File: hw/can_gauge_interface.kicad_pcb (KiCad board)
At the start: 2 copper layers, 58 parts, among them J1 USB_B, J10 Conn_01x01_Socket, J2 Conn_02x04_Top_Bottom, J3 Analog, J4 ICSP, J5 SPI debug, J6 Conn_01x01_Socket, J7 Conn_01x01_Socket, J8 Conn_01x01_Socket, J9 Conn_01x01_Socket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

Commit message: layout
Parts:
- R10, R11, R4, R6, R7, R9: footprint Resistor_SMD:R_0805_2012Metric_Pad1.20x1.40mm_HandSolder -> Resistor_THT:R_Axial_DIN0411_L9.9mm_D3.6mm_P12.70mm_Horizontal
- moved H1 344.1 mm to (33.0, 58.0)
- moved JP5 212.7 mm to (55.9, 134.6), turned to 180 degrees
- moved R8 200.3 mm to (49.8, 132.1), turned to 180 degrees
- moved R7 146.5 mm to (104.1, 121.9), turned to -90 degrees
- moved C14 145.3 mm to (78.7, 137.2), turned to 90 degrees
- moved C13 129.1 mm to (94.0, 127.0)
- moved J5 115.4 mm to (383.5, 59.3)
- moved JP3 109.4 mm to (368.3, 124.5)
- moved JP4 109.4 mm to (370.8, 111.8)
- moved J10 100.7 mm to (364.0, 77.7)
- moved J6 100.7 mm to (364.0, 59.3)
- moved J7 100.7 mm to (364.0, 63.9)
- moved J8 100.7 mm to (364.0, 68.5)
- moved J9 100.7 mm to (364.0, 73.1)
- moved R9 95.2 mm to (154.9, 142.2), turned to 180 degrees
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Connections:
- net Net-(U2-RXCAN) renamed /CAN_RX
- net Net-(U2-TXCAN) renamed /CAN_TX
- J2 pad 1: +12V -> /Tach
- J2 pad 4: /Tach -> +12V
- J2 pad 5: GND -> /Speed
- J2 pad 8: /Speed -> GND
- JP2 pad 1: Net-(JP2-A) -> /INT
- JP2 pad 2: /INT -> /INT/ICSP_CLK
- U1 pad 10: /DAC1_~{CS} -> unconnected-(U1-RB7/TX/CK-Pad10)
- U1 pad 12: /CAN_~{CS} -> unconnected-(U1-RB5/AN11/RX/DX-Pad12)
- U1 pad 14: /DAC2_~{CS} -> unconnected-(U1-C2IN2-/C1IN2-/DACOUT1/AN6/RC2-Pad14)
- U1 pad 15: Net-(JP2-A) -> /INT/ICSP_CLK
- U1 pad 2: /ROM_~{CS} -> unconnected-(U1-RA5/SOSCI/T1CKI/OSC1/CLKIN-Pad2)

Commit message: dac pullup layout
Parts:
- moved R11 286.0 mm to (73.7, 226.1), turned to 90 degrees
- moved R10 248.9 mm to (101.6, 226.1), turned to 90 degrees
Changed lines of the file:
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@@
 		(tags "THT DIP DIL PDIP 2.54mm 7.62mm 300mil")
 		(property "Reference" "U8"
-			(at -2.54 0 180)
+			(at 10.16 3.81 180)
 			(layer "F.SilkS")
 			(effects
@@
 	(footprint "Resistor_THT:R_Axial_DIN0411_L9.9mm_D3.6mm_P12.70mm_Horizontal"
 		(layer "F.Cu")
-		(at 327.66 121.92)
+		(at 101.6 226.06 90)
 		(descr "Resistor, Axial_DIN0411 series, Axial, Horizontal, pin pitch=12.7mm, 1W, length*diameter=9.9*3.6mm^2")
 		(tags "Resistor Axial_DIN0411 series Axial Horizontal pin pitch 12.7mm 1W length 9.9mm diameter 3.6mm")
 		(property "Reference" "R10"
-			(at 6.35 -2.92 0)
+			(at 5.08 5.08 180)
 			(layer "F.SilkS")
 			(effects
@@
 		)
 		(property "Value" "10k"
-			(at 6.35 2.92 0)
+			(at 6.35 2.92 90)
 			(layer "F.Fab")
+			(hide yes)
 			(effects
 				(font
@@
 		)
 		(property "Datasheet" ""
-			(at 0 0 0)
+			(at 0 0 90)
 			(unlocked yes)
 			(layer "F.Fab")
@@
 		)
 		(property "Description" "Resistor, US symbol"
-			(at 0 0 0)
+			(at 0 0 90)
 			(unlocked yes)
 			(layer "F.Fab")
@@
 		(attr through_hole)
 		(fp_line
-			(start 1.28 -1.92)
-			(end 11.42 -1.92)
+			(start 11.42 -1.92)
+			(end 11.42 -1.44)
 			(stroke
 				(width 0.12)
@@
 		)
 		(fp_line
-			(start 1.28 -1.44)
-			(end 1.28 -1.92)
+			(start 1.28 -1.92)
+			(end 11.42 -1.92)
 			(stroke
 				(width 0.12)
@@
 		)
 		(fp_line
-			(start 1.28 1.44)
-			(end 1.28 1.92)
+			(start 1.28 -1.44)
+			(end 1.28 -1.92)
 			(stroke
 				(width 0.12)
@@
 		)
 		(fp_line
-			(start 1.28 1.92)
-			(end 11.42 1.92)
+			(start 1.28 1.44)
+			(end 1.28 1.92)
 			(stroke
 				(width 0.12)
@@
 		)
 		(fp_line
-			(start 11.42 -1.92)
-			(end 11.42 -1.44)
+			(start 11.42 1.92)
+			(end 11.42 1.44)
 			(stroke
 				(width 0.12)
@@
 		)
 		(fp_line
-			(start 11.42 1.92)
-			(end 11.42 1.44)
+			(start 1.28 1.92)
+			(end 11.42 1.92)
 			(stroke
 				(width 0.12)
@@
 		)
 		(fp_line
-			(start -1.45 -2.05)
-			(end -1.45 2.05)
+			(start 14.15 -2.05)
+			(end -1.45 -2.05)
 			(stroke
 				(width 0.05)
@@
 		)
 		(fp_line
-			(start -1.45 2.05)
-			(end 14.15 2.05)
+			(start -1.45 -2.05)
+			(end -1.45 2.05)
 			(stroke
 				(width 0.05)
@@
 		)
 		(fp_line
-			(start 14.15 -2.05)
-			(end -1.45 -2.05)
+			(start 14.15 2.05)
+			(end 14.15 -2.05)
 			(stroke
 				(width 0.05)
@@
 		)
 		(fp_line
-			(start 14.15 2.05)
-			(end 14.15 -2.05)
+			(start -1.45 2.05)
+			(end 14.15 2.05)
 			(stroke
 				(width 0.05)
@@
 		)
 		(fp_line
-			(start 0 0)
-			(end 1.4 0)
+			(start 11.3 -1.8)
+			(end 1.4 -1.8)
 			(stroke
 				(width 0.1)
@@
 		)
 		(fp_line
-			(start 1.4 1.8)
-			(end 11.3 1.8)
+			(start 12.7 0)
+			(end 11.3 0)
 			(stroke
 				(width 0.1)
@@
 		)
 		(fp_line
-			(start 11.3 -1.8)
-			(end 1.4 -1.8)
+			(start 0 0)
+			(end 1.4 0)
 			(stroke
 				(width 0.1)
@@
 		)
 		(fp_line
-			(start 12.7 0)
-			(end 11.3 0)
+			(start 1.4 1.8)
+			(end 11.3 1.8)
 			(stroke
 				(width 0.1)
@@
 		)
 		(fp_text user "${REFERENCE}"
-			(at 6.35 0 0)
+			(at 6.35 0 90)
 			(layer "F.Fab")
 			(effects
@@
 		)
 		(pad "1" thru_hole circle
-			(at 0 0)
+			(at 0 0 90)
 			(size 2.4 2.4)
 			(drill 1.2)
@@
 		)
 		(pad "2" thru_hole oval
-			(at 12.7 0)
+			(at 12.7 0 90)
 			(size 2.4 2.4)
 			(drill 1.2)
@@
 	(footprint "Resistor_THT:R_Axial_DIN0411_L9.9mm_D3.6mm_P12.70mm_Horizontal"
 		(layer "F.Cu")
-		(at 342.9 129.54)
+		(at 73.66 226.06 90)
 		(descr "Resistor, Axial_DIN0411 series, Axial, Horizontal, pin pitch=12.7mm, 1W, length*diameter=9.9*3.6mm^2")
 		(tags "Resistor Axial_DIN0411 series Axial Horizontal pin pitch 12.7mm 1W length 9.9mm diameter 3.6mm")
 		(property "Reference" "R11"
-			(at 6.35 -2.92 0)
+			(at 5.08 5.08 180)
 			(layer "F.SilkS")
 			(effects
@@
 		)
 		(property "Value" "10k"
-			(at 6.35 2.92 0)
+			(at 6.35 2.92 90)
 			(layer "F.Fab")
+			(hide yes)
 			(effects
 				(font
@@
 		)
 		(property "Datasheet" ""
-			(at 0 0 0)
+			(at 0 0 90)
 			(unlocked yes)
 			(layer "F.Fab")
@@
 		)
 		(property "Description" "Resistor, US symbol"
-			(at 0 0 0)
+			(at 0 0 90)
 			(unlocked yes)
 			(layer "F.Fab")
@@
 		(attr through_hole)
 		(fp_line
-			(start 1.28 -1.92)
-			(end 11.42 -1.92)
+			(start 11.42 -1.92)
+			(end 11.42 -1.44)
 			(stroke
 				(width 0.12)
@@
 		)
 		(fp_line
-			(start 1.28 -1.44)
-			(end 1.28 -1.92)
+			(start 1.28 -1.92)
+			(end 11.42 -1.92)
 			(stroke
 				(width 0.12)
@@
 		)
 		(fp_line
-			(start 1.28 1.44)
-			(end 1.28 1.92)
+			(start 1.28 -1.44)
+			(end 1.28 -1.92)
 			(stroke
 				(width 0.12)
@@
 		)
 		(fp_line
-			(start 1.28 1.92)
-			(end 11.42 1.92)
+			(start 1.28 1.44)
+			(end 1.28 1.92)
 			(stroke
 				(width 0.12)
@@
 		)
 		(fp_line
-			(start 11.42 -1.92)
-			(end 11.42 -1.44)
+			(start 11.42 1.92)
+			(end 11.42 1.44)
 			(stroke
 				(width 0.12)
@@
 		)
 		(fp_line
-			(start 11.42 1.92)
-			(end 11.42 1.44)
+			(start 1.28 1.92)
+			(end 11.42 1.92)
 			(stroke
 				(width 0.12)
@@
 		)
 		(fp_line
-			(start -1.45 -2.05)
-			(end -1.45 2.05)
+			(start 14.15 -2.05)
+			(end -1.45 -2.05)
 			(stroke
 				(width 0.05)
@@
 		)
 		(fp_line
-			(start -1.45 2.05)
-			(end 14.15 2.05)
+			(start -1.45 -2.05)
+			(end -1.45 2.05)
 			(stroke
 				(width 0.05)
@@
 		)
 		(fp_line
-			(start 14.15 -2.05)
-			(end -1.45 -2.05)
+			(start 14.15 2.05)
+			(end 14.15 -2.05)
 			(stroke
 				(width 0.05)
@@
 		)
 		(fp_line
-			(start 14.15 2.05)
-			(end 14.15 -2.05)
+			(start -1.45 2.05)
+			(end 14.15 2.05)
 			(stroke
 				(width 0.05)
@@
 		)
 		(fp_line
-			(start 0 0)
-			(end 1.4 0)
+			(start 11.3 -1.8)
+			(end 1.4 -1.8)
 			(stroke
 				(width 0.1)
@@
 		)
 		(fp_line
-			(start 1.4 1.8)
-			(end 11.3 1.8)
+			(start 12.7 0)
+			(end 11.3 0)
 			(stroke
 				(width 0.1)
@@
 		)
 		(fp_line
-			(start 11.3 -1.8)
-			(end 1.4 -1.8)
+			(start 0 0)
+			(end 1.4 0)
 			(stroke
 				(width 0.1)
@@
 		)
 		(fp_line
-			(start 12.7 0)
-			(end 11.3 0)
+			(start 1.4 1.8)
+			(end 11.3 1.8)
 			(stroke
 				(width 0.1)
@@
 		)
 		(fp_text user "${REFERENCE}"
-			(at 6.35 0 0)
+			(at 6.35 0 90)
 			(layer "F.Fab")
 			(effects
@@
 		)
 		(pad "1" thru_hole circle
-			(at 0 0)
+			(at 0 0 90)
 			(size 2.4 2.4)
 			(drill 1.2)
@@
 		)
 		(pad "2" thru_hole oval
-			(at 12.7 0)
+			(at 12.7 0 90)
 			(size 2.4 2.4)
 			(drill 1.2)
@@
 		(tags "THT DIP DIL PDIP 2.54mm 7.62mm 300mil")
 		(property "Reference" "U9"
-			(at -2.54 0 180)
+			(at 10.16 2.54 180)
 			(layer "F.SilkS")
 			(effects

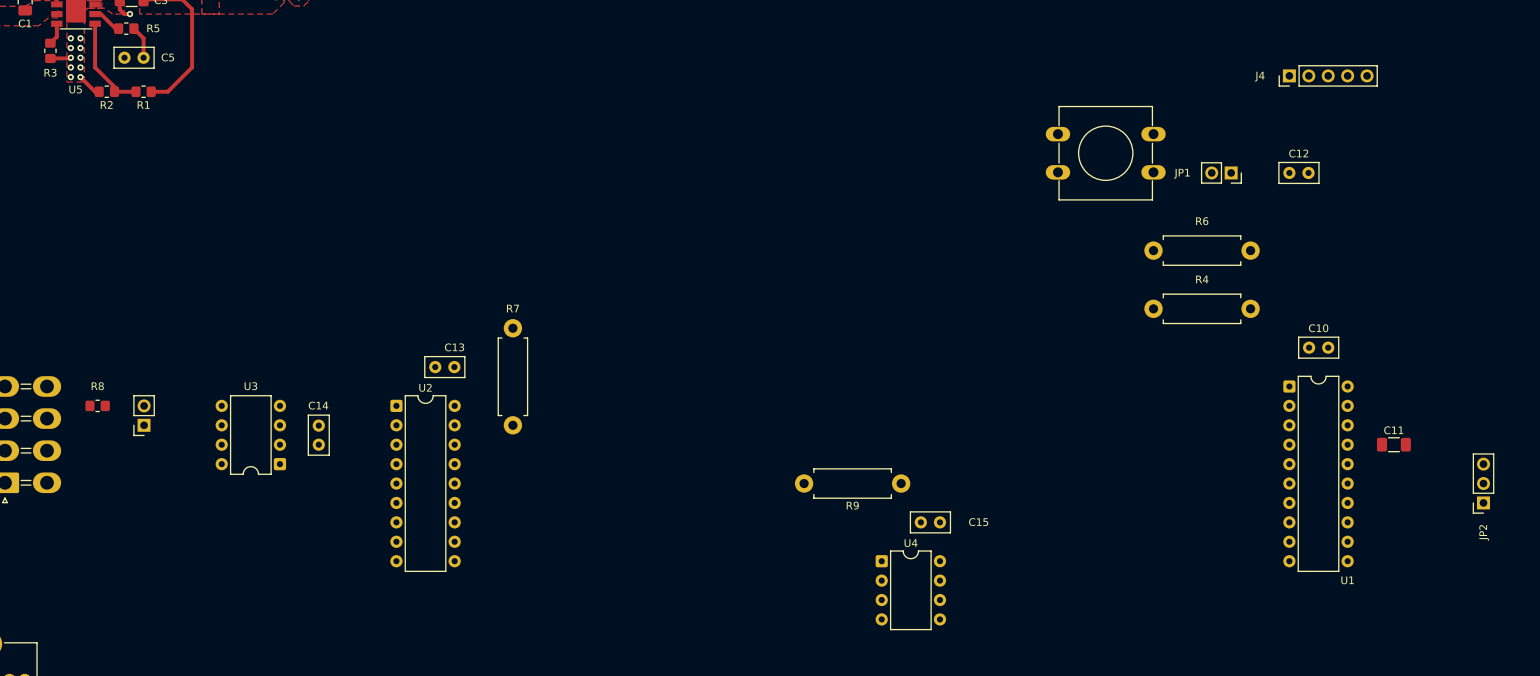
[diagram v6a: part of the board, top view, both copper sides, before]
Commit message: 4 layer stackup and CAN routing
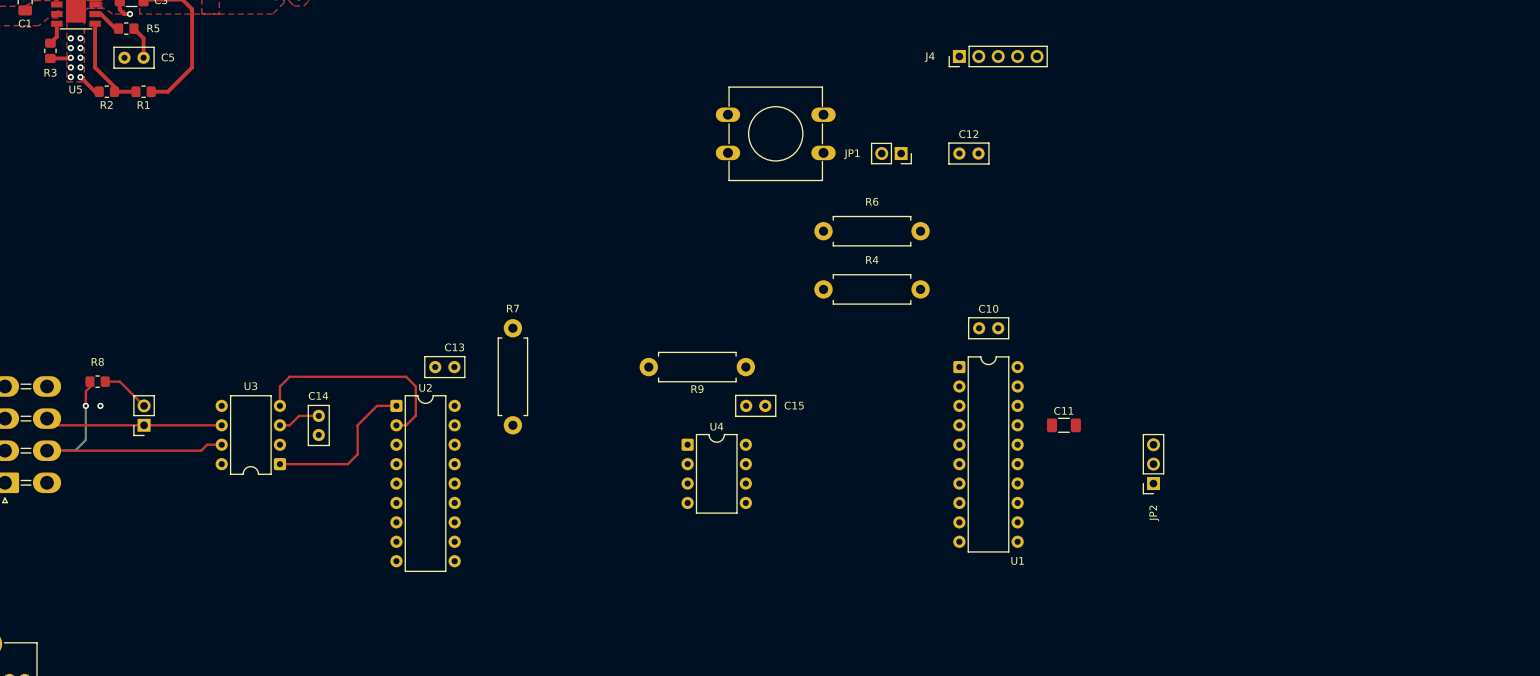
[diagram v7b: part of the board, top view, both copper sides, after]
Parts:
- moved C10 43.3 mm to (165.1, 121.9)
- moved C12 43.3 mm to (162.6, 99.1)
- moved J4 43.3 mm to (162.6, 86.4)
- moved JP1 43.3 mm to (154.9, 99.1)
- moved R4 43.3 mm to (144.8, 116.8)
- moved R6 43.3 mm to (157.5, 109.2)
- moved SW1 43.3 mm to (132.3, 94.0)
- moved U1 43.3 mm to (162.6, 127.0)
- moved C11 43.3 mm to (176.2, 134.6)
- moved JP2 43.3 mm to (188.0, 142.2)
- moved U4 29.6 mm to (127.0, 137.2)
- moved C15 27.5 mm to (137.2, 132.1)
- moved R9 25.4 mm to (134.6, 127.0)
- moved R8 3.18 mm to (49.8, 128.9)
- moved C14 1.27 mm to (78.7, 135.9)
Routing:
- net /CAN_H: track 0.00 -> 36.7 mm, vias 0 -> 1
- net /CAN_RX: track 0.00 -> 28.2 mm
- net /CAN_L: track 0.00 -> 23.2 mm
- net /CAN_TX: track 0.00 -> 20.6 mm
- net Net-(JP5-B): track 0.00 -> 6.40 mm
- net +5V: track 0.00 -> 5.59 mm
- net GND: vias 49 -> 50
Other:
- copper layers 2 -> 4

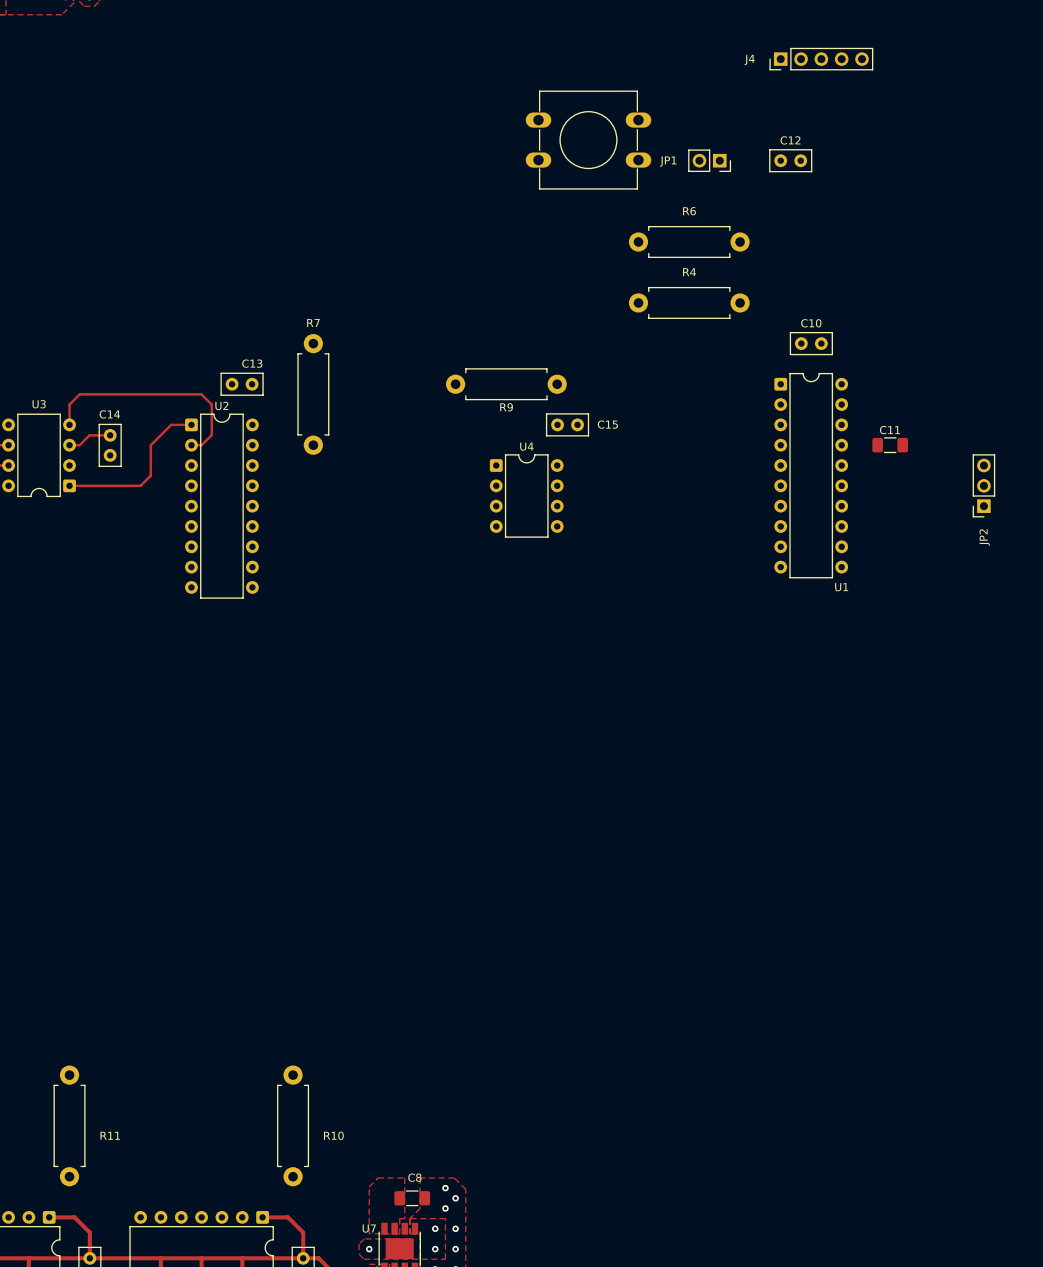
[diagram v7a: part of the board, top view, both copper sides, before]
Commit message: spi routing
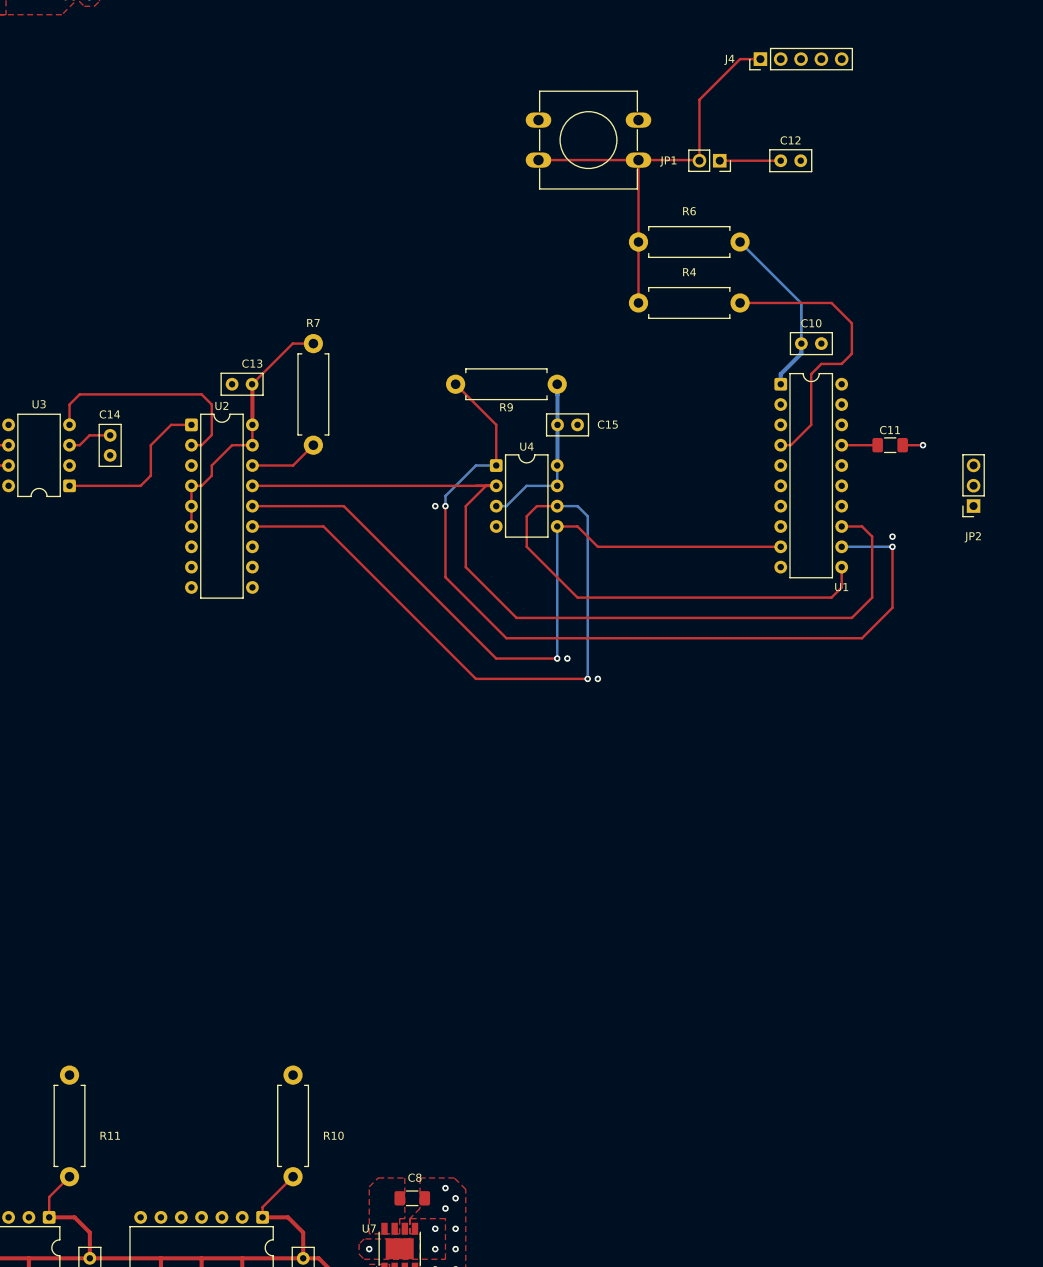
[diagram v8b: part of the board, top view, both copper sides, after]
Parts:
- moved J4 2.54 mm to (160.0, 86.4)
- moved JP2 1.30 mm to (186.7, 142.2)
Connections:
- U1 pad 12: unconnected-(U1-RB5/AN11/RX/DX-Pad12) -> /ROM_~{CS}
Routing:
- net /SCK: track 0.00 -> 127.7 mm, vias 0 -> 1
- net /MISO: track 0.00 -> 111.9 mm
- net /ROM_~{CS}: track 0.00 -> 104.9 mm, vias 0 -> 2
- net /MOSI: track 0.00 -> 91.5 mm, vias 0 -> 1
- net +5V: track 5.59 -> 82.0 mm
- net /ICSP_~{MCLR}: track 0.00 -> 55.4 mm
- net /~{MCLR}: track 0.00 -> 36.2 mm
- net +5VA: track 87.6 -> 100.4 mm
- net /CAN_~{CS}: track 0.00 -> 8.67 mm
- net Net-(JP1-A): track 0.00 -> 7.62 mm
- net Net-(U1-Vusb3v3): track 0.00 -> 4.50 mm
- net GND: track 8.85 -> 11.4 mm, vias 50 -> 55
